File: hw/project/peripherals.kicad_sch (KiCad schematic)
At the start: 71 parts, among them J1 Battery, J10 2.54 Comm, J11 Voltage Monitor, J12 SPI, J13 I2C, J14 CONN HEADER VERT 10POS 2MM, J2 Hall, J3 FTSH-107-01-L-DV-K-A, J4 Serial, J5 Phases, J8 Throttle, J9 CAN, SW3 USER, U2 ATA6561-GAQW-N

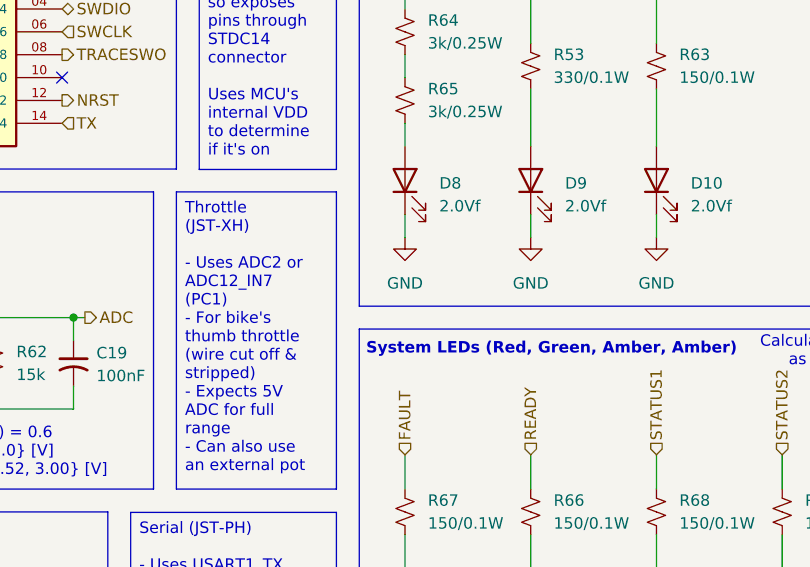
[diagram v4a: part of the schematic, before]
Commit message: Change relevant GND symbols to PGND
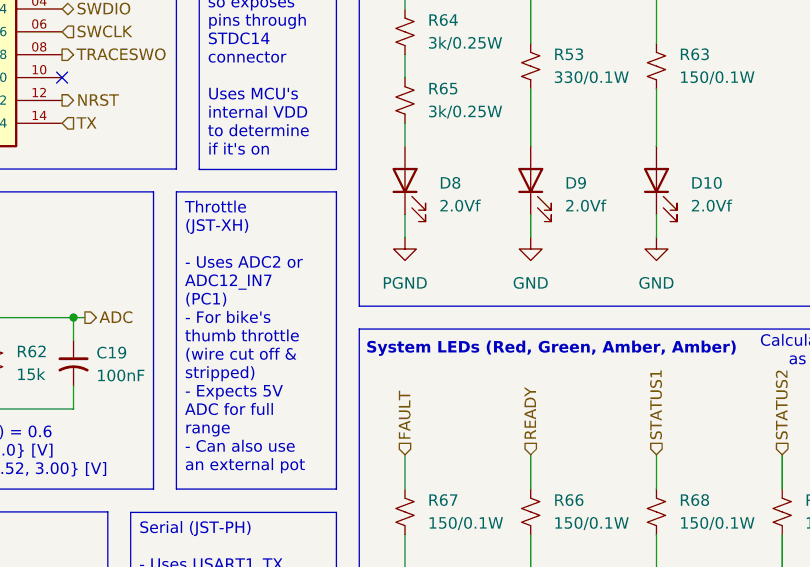
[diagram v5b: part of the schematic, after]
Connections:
- net GND: no longer D8.1 (K)
- net PGND: now also D8.1 (K)
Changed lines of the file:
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@@
+	)
+	(symbol
+		(lib_id "power:GND")
+		(at 243.84 55.88 0)
+		(unit 1)
+		(body_style 1)
+		(exclude_from_sim no)
+		(in_bom yes)
+		(on_board yes)
+		(in_pos_files yes)
+		(dnp no)
+		(fields_autoplaced yes)
+		(property "Reference" "#PWR018"
+			(at 243.84 62.23 0)
+			(hide yes)
+			(show_name no)
+			(do_not_autoplace no)
+			(effects
+				(font
+					(size 1.27 1.27)
+				)
+			)
+		)
+		(property "Value" "PGND"
+			(at 243.84 60.96 0)
+			(show_name no)
+			(do_not_autoplace no)
+			(effects
+				(font
+					(size 1.27 1.27)
+				)
+			)
+		)
+		(property "Footprint" ""
+			(at 243.84 55.88 0)
+			(hide yes)
+			(show_name no)
+			(do_not_autoplace no)
+			(effects
+				(font
+					(size 1.27 1.27)
+				)
+			)
+		)
+		(property "Datasheet" ""
+			(at 243.84 55.88 0)
+			(hide yes)
+			(show_name no)
+			(do_not_autoplace no)
+			(effects
+				(font
+					(size 1.27 1.27)
+				)
+			)
+		)
+		(property "Description" "Power symbol creates a global label with name \"GND\" , ground"
+			(at 243.84 55.88 0)
+			(hide yes)
+			(show_name no)
+			(do_not_autoplace no)
+			(effects
+				(font
+					(size 1.27 1.27)
+				)
+			)
+		)
+		(pin "1"
+		)
+		(instances
+			(project "esc"
+				(path "/86a17c4d-db96-42a1-af84-d43fe593f4e6/84ea8536-46c8-4cae-8743-a6718dee2882"
+					(reference "#PWR018")
+					(unit 1)
+				)
+			)
+		)
 	)
 	(symbol
@@
 					(unit 1)
 				)
-			)
-		)
-	)
-	(symbol
-		(lib_id "power:GND")
-		(at 243.84 55.88 0)
-		(unit 1)
-		(body_style 1)
-		(exclude_from_sim no)
-		(in_bom yes)
-		(on_board yes)
-		(in_pos_files yes)
-		(dnp no)
-		(fields_autoplaced yes)
-		(property "Reference" "#PWR0107"
-			(at 243.84 62.23 0)
-			(hide yes)
-			(show_name no)
-			(do_not_autoplace no)
-			(effects
-				(font
-					(size 1.27 1.27)
-				)
-			)
-		)
-		(property "Value" "GND"
-			(at 243.84 60.96 0)
-			(show_name no)
-			(do_not_autoplace no)
-			(effects
-				(font
-					(size 1.27 1.27)
-				)
-			)
-		)
-		(property "Footprint" ""
-			(at 243.84 55.88 0)
-			(hide yes)
-			(show_name no)
-			(do_not_autoplace no)
-			(effects
-				(font
-					(size 1.27 1.27)
-				)
-			)
-		)
-		(property "Datasheet" ""
-			(at 243.84 55.88 0)
-			(hide yes)
-			(show_name no)
-			(do_not_autoplace no)
-			(effects
-				(font
-					(size 1.27 1.27)
-				)
-			)
-		)
-		(property "Description" "Power symbol creates a global label with name \"GND\" , ground"
-			(at 243.84 55.88 0)
-			(hide yes)
-			(show_name no)
-			(do_not_autoplace no)
-			(effects
-				(font
-					(size 1.27 1.27)
-				)
-			)
-		)
-		(pin "1"
-		)
-		(instances
-			(project "esc"
-				(path "/86a17c4d-db96-42a1-af84-d43fe593f4e6/84ea8536-46c8-4cae-8743-a6718dee2882"
-					(reference "#PWR0107")
-					(unit 1)
-				)

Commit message: Prep to revamp power sheet
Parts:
- removed C19: 100nF, symbol Device:C_Small_US
- removed C47: 100nF/25V, Capacitor_SMD:C_0805_2012Metric_Pad1.18x1.45mm_HandSolder, symbol Device:C_Small
- removed C63: 1nF, Capacitor_SMD:C_0603_1608Metric, symbol Device:C_Small
- removed J11: Voltage Monitor, Connector_PinHeader_2.54mm:PinHeader_1x04_P2.54mm_Vertical, symbol Connector_Generic:Conn_01x04
- removed R44, R45, R46, R47, R48, R49, R56, R57: 10k, Resistor_SMD:R_0805_2012Metric_Pad1.20x1.40mm_HandSolder, symbol Device:R_Small_US
- removed R58: 0, Resistor_SMD:R_0805_2012Metric_Pad1.20x1.40mm_HandSolder, symbol Device:R_Small_US
- removed R59: DNP, Resistor_SMD:R_0805_2012Metric_Pad1.20x1.40mm_HandSolder, symbol Device:R_Small_US
- removed R71: 100k, symbol Device:R_Small_US
- added C19, C32, C34: 0.1uF, Capacitor_SMD:C_0603_1608Metric, symbol Device:C_Small
- added J15: Voltage Monitor, Connector_PinHeader_2.54mm:PinHeader_1x04_P2.54mm_Vertical, symbol Connector_Generic:Conn_01x04
- added R100, R101, R104, R106, R107, R95, R96, R97, R98, R99: 10k, Resistor_SMD:R_0603_1608Metric, symbol Device:R_Small_US
- added R102: DNP, Resistor_SMD:R_0603_1608Metric, symbol Device:R_Small_US
- J10: footprint (none) -> Connector_PinSocket_2.54mm:PinSocket_1x05_P2.54mm_Vertical
- J4: footprint Connector_JST:JST_PH_B4B-PH-K_1x04_P2.00mm_Vertical -> Connector_JST:JST_XH_B4B-XH-A_1x04_P2.50mm_Vertical
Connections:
- net 5V: now also J15.2 (Pin_2), R101.1
- net ADC: now also C34.1, R106.2
- net ADC_IN: now also R106.1
- net GND: now also C19.1, C32.2, C34.2, J15.4 (Pin_4), R107.2
- net HA: now also R98.2
- net HB: now also R99.2
- net HC: now also R100.2
- net VCC: now also J15.1 (Pin_1)
- net VDD: now also J15.3 (Pin_3), R102.1, R95.1, R96.1, R97.1
- net VM: now also R104.1
- net at S1.1: now also R104.2
- net at J2.5 (Pin_5): now also R100.1, R97.2
- net at R73.2, SW3.2: now also C19.2, R107.1
- net at J2.3 (Pin_3): now also R95.2, R98.1
- net at J2.1 (Pin_1): now also C32.1, R101.2, R102.2
- net at J2.4 (Pin_4): now also R96.2, R99.1
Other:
- moved on the sheet: J9, TP8, TP9

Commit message: Continuing power revamp tomorrow
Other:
- note added: "TO-SPEC STILL!!"
- note added: "remove?"
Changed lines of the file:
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@@
 		)
 	)
+	(text "TO-SPEC STILL!!"
+		(exclude_from_sim no)
+		(at 205.994 55.118 0)
+		(effects
+			(font
+				(size 1.27 1.27)
+				(color 255 4 4 1)
+			)
+		)
+	)
 	(text "CANBus Split Termination"
 		(exclude_from_sim no)
@@
 		)
 	)
+	(text "TO-SPEC STILL!!"
+		(exclude_from_sim no)
+		(at 282.702 118.11 0)
+		(effects
+			(font
+				(size 1.27 1.27)
+				(color 255 4 4 1)
+			)
+		)
+	)
 	(text "Power Switch"
 		(exclude_from_sim no)
@@
 		)
 	)
+	(text "TO-SPEC STILL!!"
+		(exclude_from_sim no)
+		(at 297.942 75.438 0)
+		(effects
+			(font
+				(size 1.27 1.27)
+				(color 255 4 4 1)
+			)
+		)
+	)
 	(text "CAN Transceiver"
 		(exclude_from_sim no)
@@
 		)
 	)
+	(text "TO-SPEC STILL!!"
+		(exclude_from_sim no)
+		(at 287.274 31.496 0)
+		(effects
+			(font
+				(size 1.27 1.27)
+				(color 255 4 4 1)
+			)
+		)
+	)
 	(text "update pin references"
 		(exclude_from_sim no)
@@
 		)
 	)
+	(text "remove?"
+		(exclude_from_sim no)
+		(at 15.748 25.4 0)
+		(effects
+			(font
+				(size 1.27 1.27)
+				(color 255 4 4 1)
+			)
+		)
+	)
 	(text "SPI (SPI1)"
 		(exclude_from_sim no)
@@
 			)
 		)
-		(property "Datasheet" "https://www.we-online.com/catalog/datasheet/691256610002.pdf"
+		(property "Datasheet" "https://www.digikey.ca/en/products/detail/w%C3%BCrth-elektronik/691256610002/6644127"
 			(at 38.1 62.23 0)
 			(hide yes)
@@
 			)
 		)
-		(property "Description" ""
+		(property "Description" "TERM BLK 2P SIDE ENT 10.16MM PCB"
 			(at 38.1 62.23 0)
 			(hide yes)
@@
 			)
 		)
-		(property "Datasheet" "https://www.we-online.com/catalog/datasheet/691256610003.pdf"
+		(property "Datasheet" "https://www.digikey.ca/en/products/detail/w%C3%BCrth-elektronik/691256610003/6644128"
 			(at 77.47 33.02 0)
 			(hide yes)
@@
 			)
 		)
-		(property "Description" ""
+		(property "Description" "TERM BLK 3P SIDE ENT 10.16MM PCB"
 			(at 77.47 33.02 0)
 			(hide yes)

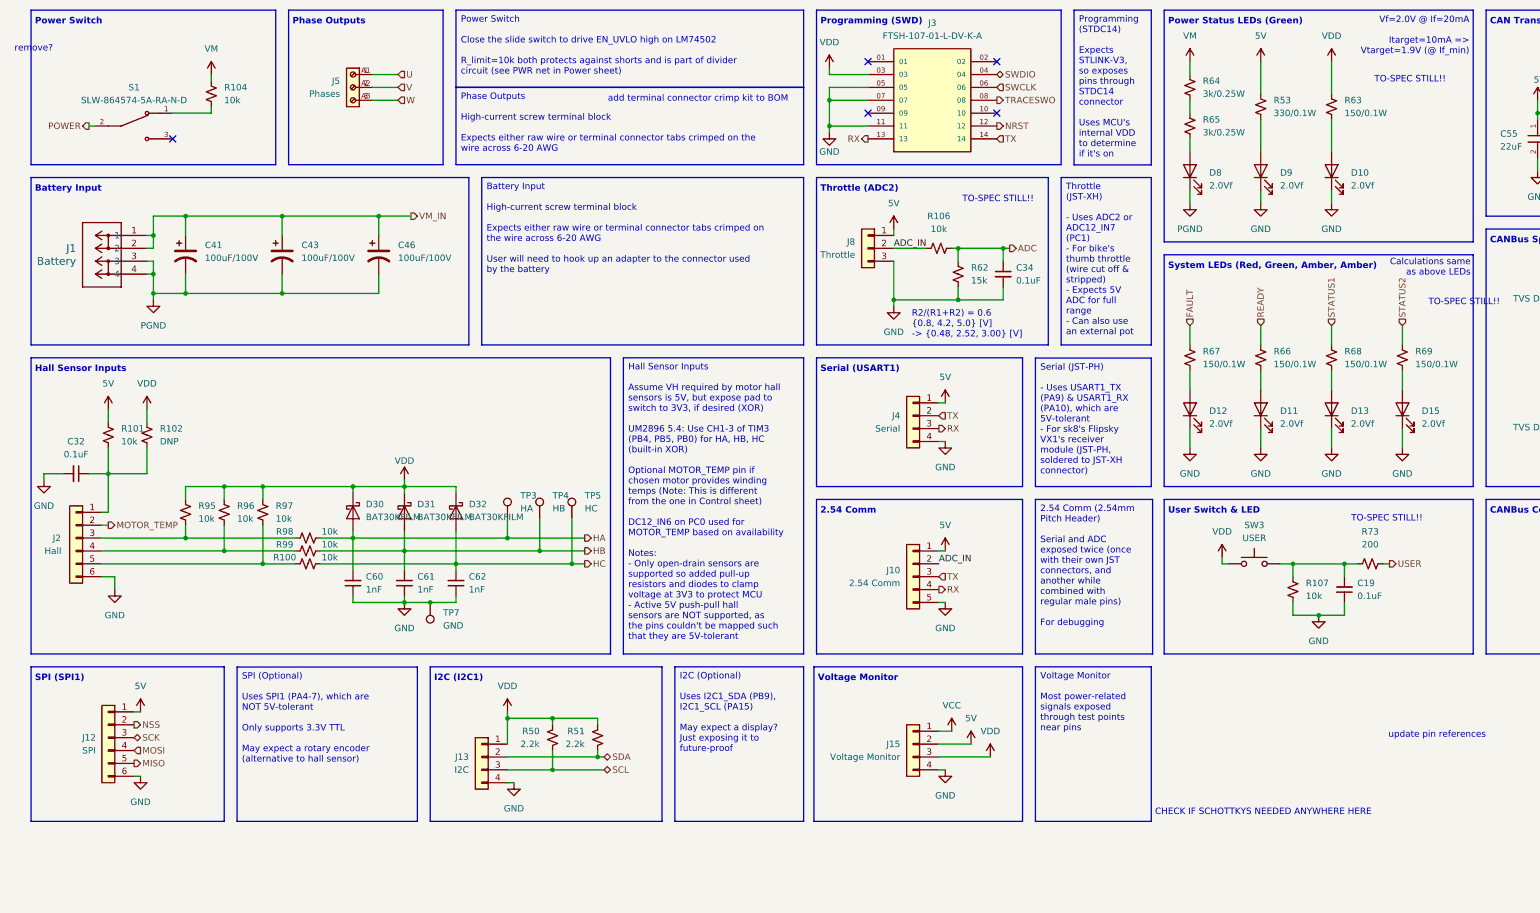
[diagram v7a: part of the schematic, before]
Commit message: First draft of power revamp
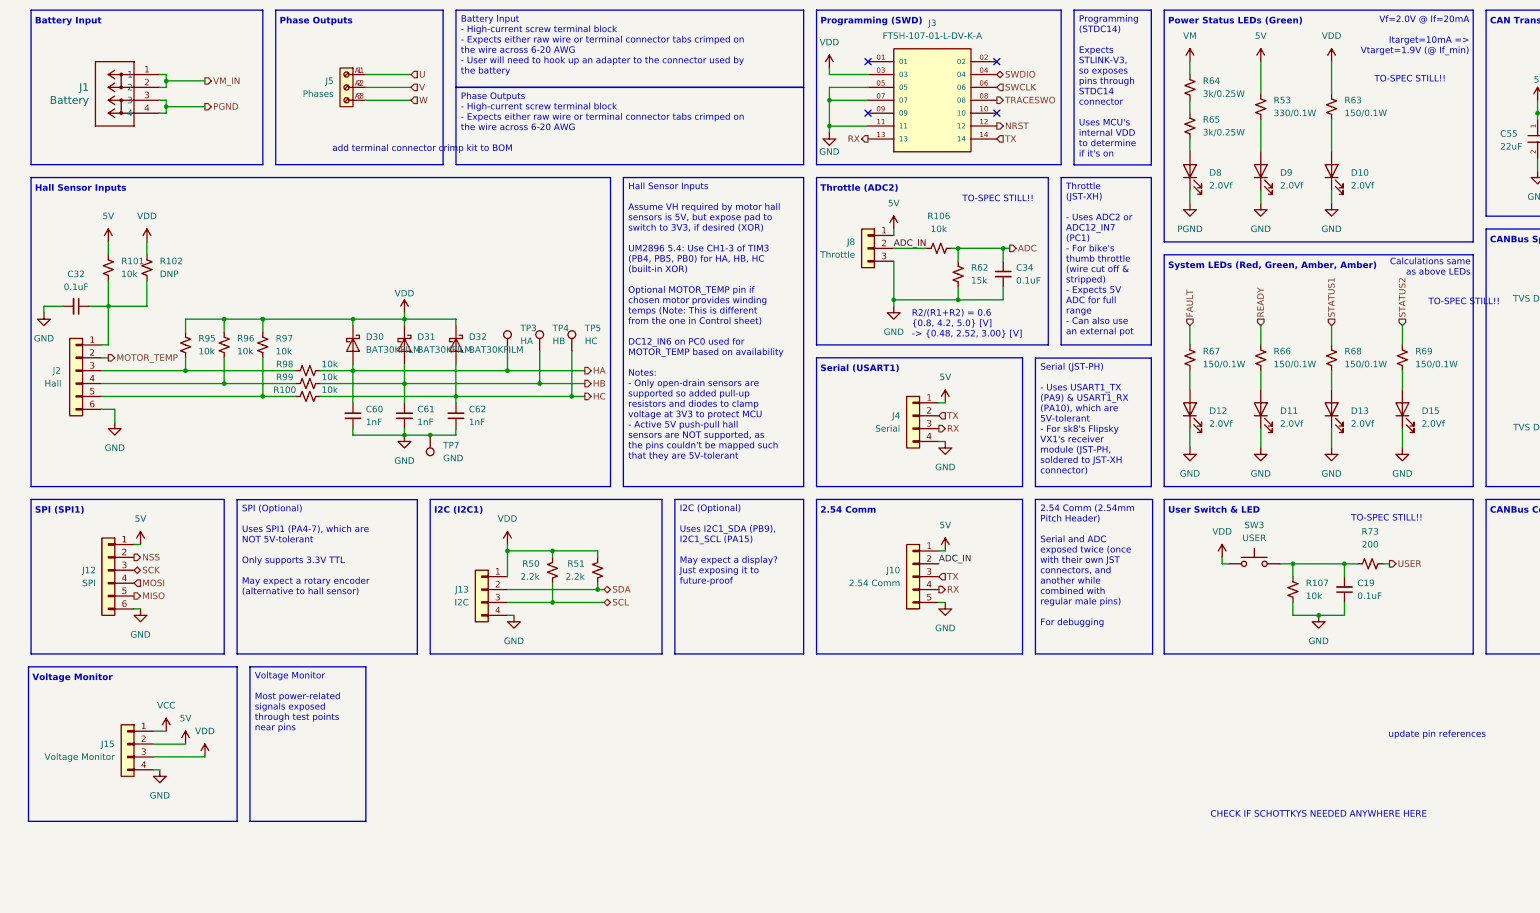
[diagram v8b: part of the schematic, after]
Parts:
- removed C41, C43, C46: 100uF/100V, EKY_101ETD101MJ20S:CAP_J20_NIP, symbol Device:C_Polarized_US
- removed R104: 10k, Resistor_SMD:R_0603_1608Metric, symbol Device:R_Small_US
- removed S1: SLW-864574-5A-RA-N-D, SLW-864574-5A-RA-N-D:SW_SLW-864574-5A-RA-N-D, symbol SLW-864574-5A-RA-N-D:SLW-864574-5A-RA-N-D
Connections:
- no-connect marks 5 -> 4
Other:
- note removed: "Power Switch"
- note removed: "remove?"
- moved on the sheet: C32, C60, C61, C62, D30, D31, D32, J1, J12, J13, J15, J2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
